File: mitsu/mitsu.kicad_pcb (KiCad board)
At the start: 2 copper layers, 8 parts, among them J1 Conn_Coaxial, J2 Conn_Coaxial

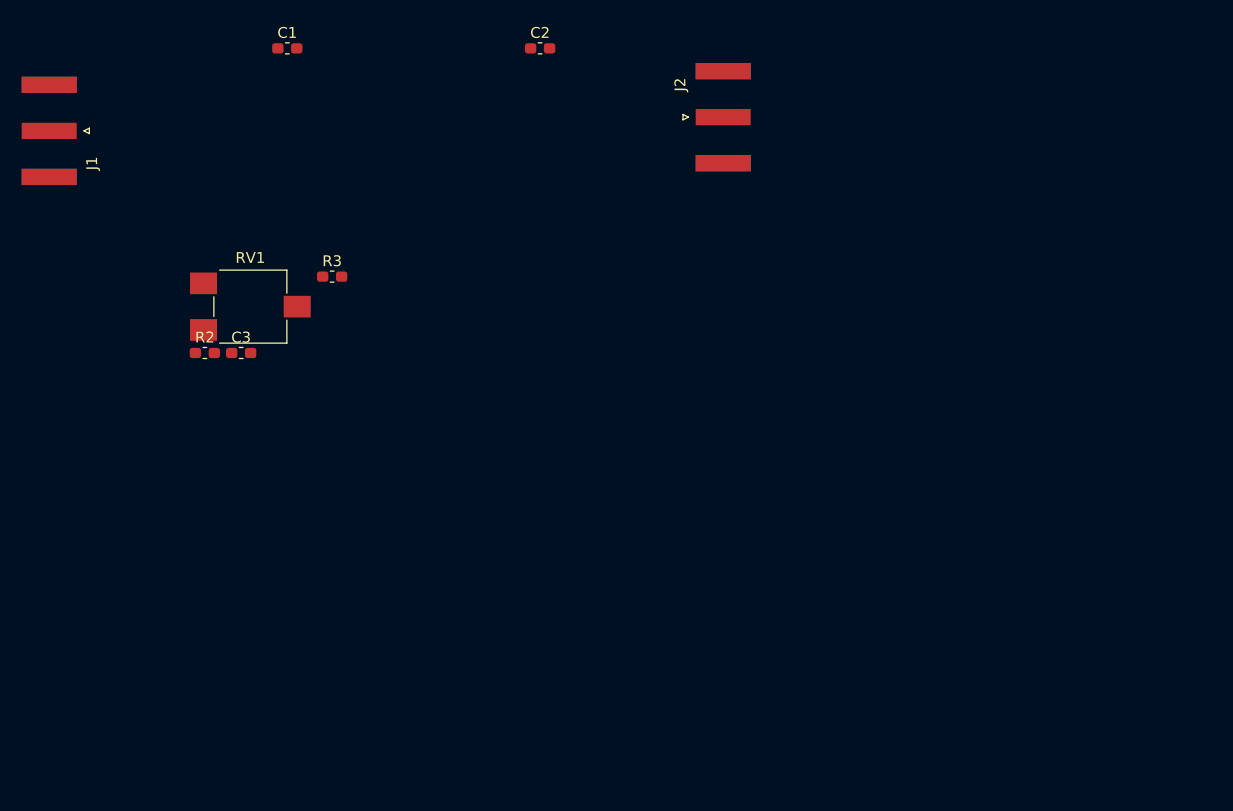
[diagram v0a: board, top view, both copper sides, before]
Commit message: fixed PA footprint
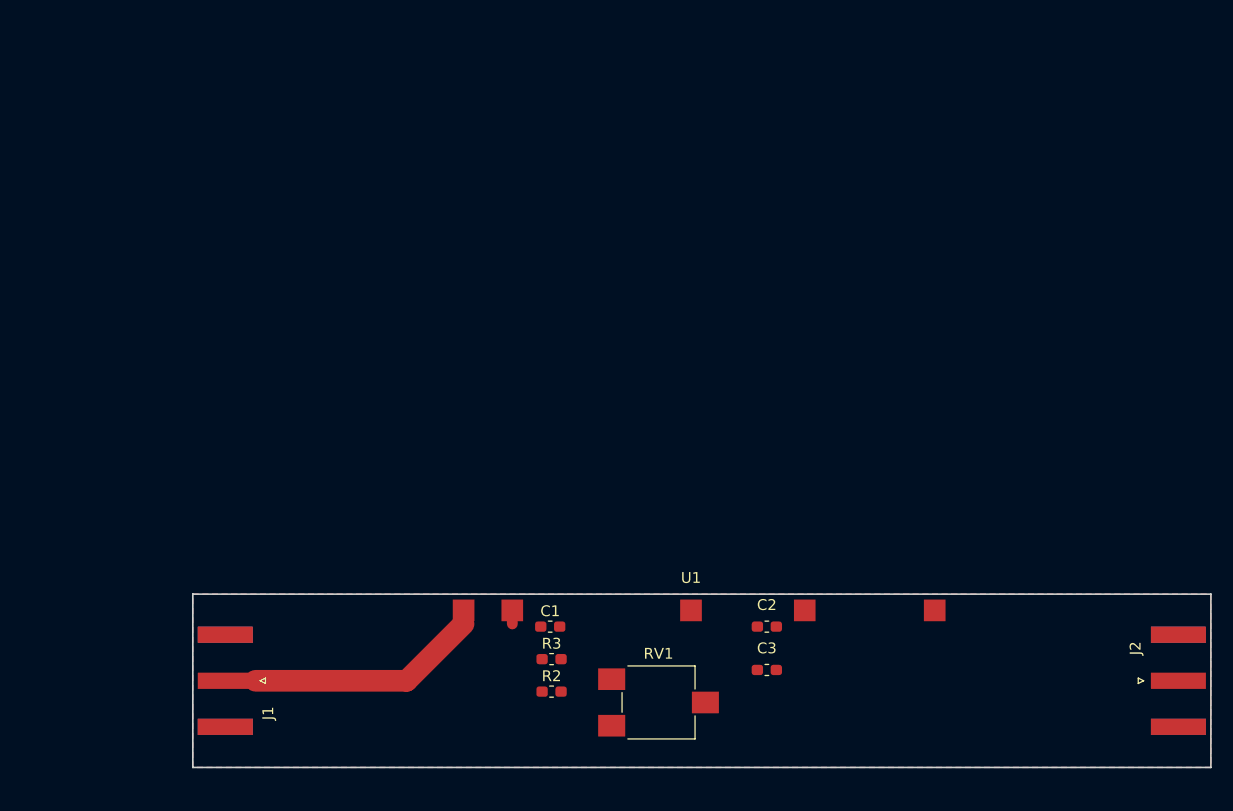
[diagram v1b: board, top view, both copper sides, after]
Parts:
- added U1: MPA, drom:MPA, F.Cu at (138.0, 105.0)
- moved J2 66.9 mm to (183.0, 113.0)
- moved C1 58.6 mm to (125.0, 108.0)
- moved C2 57.3 mm to (145.0, 108.0), turned to 180 degrees
- moved C3 56.7 mm to (145.0, 112.0), turned to 180 degrees
- moved J1 53.3 mm to (95.0, 113.0)
- moved RV1 52.5 mm to (135.0, 115.0)
- moved R2 44.7 mm to (125.1, 114.0)
- moved R3 40.7 mm to (125.1, 111.0)
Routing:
- net Net-(J1-Pad1): track 0.00 -> 25.4 mm
- net Net-(C1-Pad1): track 0.00 -> 1.25 mm
- added copper zone on B.Cu, net GNDPWR
- added copper zone on F.Cu, net GNDPWR
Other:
- board outline added: 94 x 16 mm
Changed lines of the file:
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@@
   (general
     (thickness 1.6)
-    (drawings 0)
-    (tracks 0)
+    (drawings 4)
+    (tracks 5)
     (zones 0)
-    (modules 8)
+    (modules 9)
     (nets 7)
   )
@@
     (add_net "Net-(R2-Pad2)")
   )
+  (module drom:MPA (layer F.Cu)
+    (at 138 105)
+    (descr "8-Lead Plastic PSOP, Exposed Die Pad (TI DDA0008B, see http://www.ti.com/lit/ds/symlink/lm3404.pdf)")
+    (tags "SSOP 0.50 exposed pad")
+    (attr smd)
+    (fp_text reference U1 (at 0 -1.5) (layer F.SilkS)
+      (effects (font (size 1 1) (thickness 0.15)))
+    )
+    (fp_text value MPA (at 0 -8) (layer F.Fab)
+      (effects (font (size 1 1) (thickness 0.15)))
+    )
+    (fp_text user %R (at 0 -3.5) (layer F.Fab)
+      (effects (font (size 1 1) (thickness 0.15)))
+    )
+    (fp_line (start -25 0) (end -25 -19) (layer F.Fab) (width 0.15))
+    (fp_line (start -25 -19) (end 25 -19) (layer F.Fab) (width 0.15))
+    (fp_line (start 25 -19) (end 25 0) (layer F.Fab) (width 0.15))
+    (fp_line (start 25 0) (end -25 0) (layer F.Fab) (width 0.15))
+    (fp_line (start -25 -0.5) (end -33.5 -0.5) (layer F.Fab) (width 0.15))
+    (fp_line (start -33.5 -0.5) (end -33.5 -8) (layer F.Fab) (width 0.15))
+    (fp_line (start -30.5 -18.5) (end -25 -18.5) (layer F.Fab) (width 0.15))
+    (fp_line (start -33.5 -8) (end -30 -8) (layer F.Fab) (width 0.15))
+    (fp_line (start -30 -12) (end -33.5 -12) (layer F.Fab) (width 0.15))
+    (fp_arc (start -30 -10) (end -30 -8) (angle -180) (layer F.Fab) (width 0.15))
+    (fp_line (start -33.5 -12) (end -33.5 -15.5) (layer F.Fab) (width 0.15))
+    (fp_line (start -33.5 -15.5) (end -30.5 -18.5) (layer F.Fab) (width 0.15))
+    (fp_line (start 33.5 -12) (end 30 -12) (layer F.Fab) (width 0.15))
+    (fp_arc (start 30 -10) (end 30 -12) (angle -180) (layer F.Fab) (width 0.15))
+    (fp_line (start 25 -18.5) (end 30.5 -18.5) (layer F.Fab) (width 0.15))
+    (fp_line (start 30 -8) (end 33.5 -8) (layer F.Fab) (width 0.15))
+    (fp_line (start 33.5 -0.5) (end 25 -0.5) (layer F.Fab) (width 0.15))
+    (fp_line (start 33.5 -15.5) (end 30.5 -18.5) (layer F.Fab) (width 0.15))
+    (fp_line (start 33.5 -12) (end 33.5 -15.5) (layer F.Fab) (width 0.15))
+    (fp_line (start 33.5 -0.5) (end 33.5 -8) (layer F.Fab) (width 0.15))
+    (pad 1 smd rect (at -21 1.5) (size 2 2) (layers F.Cu F.Paste F.Mask)
+      (net 2 "Net-(J1-Pad1)"))
+    (pad 2 smd rect (at -16.5 1.5) (size 2 2) (layers F.Cu F.Paste F.Mask)
+      (net 4 "Net-(C1-Pad1)"))
+    (pad 3 smd rect (at 10.5 1.5) (size 2 2) (layers F.Cu F.Paste F.Mask)
+      (net 6 +12V))
+    (pad 4 smd rect (at 22.5 1.5) (size 2 2) (layers F.Cu F.Paste F.Mask)
+      (net 3 "Net-(J2-Pad1)"))
+    (pad 5 smd rect (at 0 1.5) (size 2 2) (layers F.Cu F.Paste F.Mask)
+      (net 1 GNDPWR))
+    (model ${KISYS3DMOD}/Package_SO.3dshapes/TI_SO-PowerPAD-8.wrl
+      (at (xyz 0 0 0))
+      (scale (xyz 1 1 1))
+      (rotate (xyz 0 0 0))
+    )
+  )
   (module Capacitor_SMD:C_0603_1608Metric_Pad1.05x0.95mm_HandSolder (layer F.Cu)
-    (at 96.465001 82.735001)
+    (at 145 112 180)
     (descr "Capacitor SMD 0603 (1608 Metric), square (rectangular) end terminal, IPC_7351 nominal with elongated pad for handsoldering. (Body size source: http://www.tortai-tech.com/upload/download/2011102023233369053.pdf), generated with kicad-footprint-generator")
     (tags "capacitor handsolder")
     (attr smd)
-    (fp_text reference C3 (at 0 -1.43) (layer F.SilkS)
-      (effects (font (size 1 1) (thickness 0.15)))
-    )
-    (fp_text value C (at 0 1.43) (layer F.Fab)
+    (fp_text reference C3 (at 0 2 180) (layer F.SilkS)
+      (effects (font (size 1 1) (thickness 0.15)))
+    )
+    (fp_text value C (at -2 0 180) (layer F.Fab)
       (effects (font (size 1 1) (thickness 0.15)))
     )
@@
     (fp_line (start 1.65 -0.73) (end 1.65 0.73) (layer F.CrtYd) (width 0.05))
     (fp_line (start 1.65 0.73) (end -1.65 0.73) (layer F.CrtYd) (width 0.05))
-    (fp_text user %R (at 0 0) (layer F.Fab)
+    (fp_text user %R (at 0.534999 0 180) (layer F.Fab)
       (effects (font (size 0.4 0.4) (thickness 0.06)))
     )
-    (pad 1 smd roundrect (at -0.875 0) (size 1.05 0.95) (layers F.Cu F.Paste F.Mask) (roundrect_rratio 0.25)
+    (pad 1 smd roundrect (at -0.875 0 180) (size 1.05 0.95) (layers F.Cu F.Paste F.Mask) (roundrect_rratio 0.25)
       (net 6 +12V))
-    (pad 2 smd roundrect (at 0.875 0) (size 1.05 0.95) (layers F.Cu F.Paste F.Mask) (roundrect_rratio 0.25)
+    (pad 2 smd roundrect (at 0.875 0 180) (size 1.05 0.95) (layers F.Cu F.Paste F.Mask) (roundrect_rratio 0.25)
       (net 1 GNDPWR))
     (model ${KISYS3DMOD}/Capacitor_SMD.3dshapes/C_0603_1608Metric.wrl
@@
   )
   (module Potentiometer_SMD:Potentiometer_ACP_CA6-VSMD_Vertical (layer F.Cu)
-    (at 97.315001 78.455001)
+    (at 135 115)
     (descr "Potentiometer, vertical, ACP CA6-VSMD, http://www.acptechnologies.com/wp-content/uploads/2017/06/01-ACP-CA6.pdf")
     (tags "Potentiometer vertical ACP CA6-VSMD")
@@
   )
   (module Resistor_SMD:R_0603_1608Metric_Pad1.05x0.95mm_HandSolder (layer F.Cu)
-    (at 104.865001 75.685001)
+    (at 125.125 111)
     (descr "Resistor SMD 0603 (1608 Metric), square (rectangular) end terminal, IPC_7351 nominal with elongated pad for handsoldering. (Body size source: http://www.tortai-tech.com/upload/download/2011102023233369053.pdf), generated with kicad-footprint-generator")
     (tags "resistor handsolder")
@@
   )
   (module Resistor_SMD:R_0603_1608Metric_Pad1.05x0.95mm_HandSolder (layer F.Cu)
-    (at 93.115001 82.735001)
+    (at 125.125 114)
     (descr "Resistor SMD 0603 (1608 Metric), square (rectangular) end terminal, IPC_7351 nominal with elongated pad for handsoldering. (Body size source: http://www.tortai-tech.com/upload/download/2011102023233369053.pdf), generated with kicad-footprint-generator")
     (tags "resistor handsolder")
@@
   )
   (module Capacitor_SMD:C_0603_1608Metric_Pad1.05x0.95mm_HandSolder (layer F.Cu)
-    (at 124.065 54.61)
+    (at 145 108 180)
     (descr "Capacitor SMD 0603 (1608 Metric), square (rectangular) end terminal, IPC_7351 nominal with elongated pad for handsoldering. (Body size source: http://www.tortai-tech.com/upload/download/2011102023233369053.pdf), generated with kicad-footprint-generator")
     (tags "capacitor handsolder")
     (attr smd)
-    (fp_text reference C2 (at 0 -1.43) (layer F.SilkS)
+    (fp_text reference C2 (at 0 2 180) (layer F.SilkS)
       (effects (font (size 1 1) (thickness 0.15)))
     )
@@
       (effects (font (size 1 1) (thickness 0.15)))
     )
-    (fp_text user %R (at 0 0) (layer F.Fab)
+    (fp_text user %R (at -19.065 21.39 180) (layer F.Fab)
       (effects (font (size 0.4 0.4) (thickness 0.06)))
     )
@@
     (fp_line (start -0.8 -0.4) (end 0.8 -0.4) (layer F.Fab) (width 0.1))
     (fp_line (start -0.8 0.4) (end -0.8 -0.4) (layer F.Fab) (width 0.1))
-    (pad 2 smd roundrect (at 0.875 0) (size 1.05 0.95) (layers F.Cu F.Paste F.Mask) (roundrect_rratio 0.25)
-      (net 1 GNDPWR))
-    (pad 1 smd roundrect (at -0.875 0) (size 1.05 0.95) (layers F.Cu F.Paste F.Mask) (roundrect_rratio 0.25)
+    (pad 2 smd roundrect (at 0.875 0 180) (size 1.05 0.95) (layers F.Cu F.Paste F.Mask) (roundrect_rratio 0.25)
+      (net 1 GNDPWR))
+    (pad 1 smd roundrect (at -0.875 0 180) (size 1.05 0.95) (layers F.Cu F.Paste F.Mask) (roundrect_rratio 0.25)
       (net 6 +12V))
     (model ${KISYS3DMOD}/Capacitor_SMD.3dshapes/C_0603_1608Metric.wrl
@@
   )
   (module Capacitor_SMD:C_0603_1608Metric_Pad1.05x0.95mm_HandSolder (layer F.Cu)
-    (at 100.725 54.61)
+    (at 125 108)
     (descr "Capacitor SMD 0603 (1608 Metric), square (rectangular) end terminal, IPC_7351 nominal with elongated pad for handsoldering. (Body size source: http://www.tortai-tech.com/upload/download/2011102023233369053.pdf), generated with kicad-footprint-generator")
     (tags "capacitor handsolder")
@@
   )
   (module Connector_Coaxial:SMA_Amphenol_132289_EdgeMount (layer F.Cu)
-    (at 140.97 60.96)
+    (at 183 113)
     (descr http://www.amphenolrf.com/132289.html)
     (tags SMA)
@@
   )
   (module Connector_Coaxial:SMA_Amphenol_132289_EdgeMount (layer F.Cu)
-    (at 78.74 62.23 180)
+    (at 95 113 180)
     (descr http://www.amphenolrf.com/132289.html)
     (tags SMA)
@@
     )
   )
+  (gr_line (start 92 121) (end 92 105) (layer Edge.Cuts) (width 0.15))
+  (gr_line (start 186 121) (end 92 121) (layer Edge.Cuts) (width 0.15))
+  (gr_line (start 186 105) (end 186 121) (layer Edge.Cuts) (width 0.15))
+  (gr_line (start 92 105) (end 186 105) (layer Edge.Cuts) (width 0.15))
+  (segment (start 117 107.75) (end 111.75 113) (width 2) (layer F.Cu) (net 2))
+  (segment (start 97.79 113) (end 95 113) (width 0.25) (layer F.Cu) (net 2))
+  (segment (start 111.75 113) (end 97.79 113) (width 2) (layer F.Cu) (net 2))
+  (segment (start 117 106.5) (end 117 107.75) (width 1) (layer F.Cu) (net 2))
+  (segment (start 121.5 106.5) (end 121.5 107.75) (width 1) (layer F.Cu) (net 4))
+  (zone (net 1) (net_name GNDPWR) (layer B.Cu) (hatch edge 0.508)
+    (connect_pads (clearance 0.508))
+    (min_thickness 0.254)
+    (fill yes (arc_segments 16) (thermal_gap 0.508) (thermal_bridge_width 0.508))
+    (polygon
+      (pts
+        (xy 92 105) (xy 186 105) (xy 186 121) (xy 92 121)
+      )
+    )
+  )
+  (zone (net 1) (net_name GNDPWR) (layer F.Cu) (hatch edge 0.508)
+    (connect_pads (clearance 0.508))
+    (min_thickness 0.254)
+    (fill yes (arc_segments 16) (thermal_gap 0.508) (thermal_bridge_width 0.508))
+    (polygon
+      (pts
+        (xy 92 105) (xy 186 105) (xy 186 121) (xy 92 121)
+      )
+    )
+  )

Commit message: v1.0
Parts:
- added C10: 7.5, Capacitor_SMD:C_0805_2012Metric_Pad1.15x1.40mm_HandSolder, F.Cu at (171.0, 115.0)
- added C11: 4.7, Capacitor_SMD:C_0805_2012Metric_Pad1.15x1.40mm_HandSolder, F.Cu at (176.0, 115.0)
- added C4: 4700, Capacitor_SMD:C_0603_1608Metric_Pad1.05x0.95mm_HandSolder, F.Cu at (145.0, 106.0)
- added C5: 22.0, Capacitor_SMD:C_1210_3225Metric, F.Cu at (124.6, 109.0)
- added C6: 22.0, Capacitor_SMD:C_1210_3225Metric, F.Cu at (145.0, 109.0)
- added C7: 0.1, Capacitor_SMD:C_0603_1608Metric_Pad1.05x0.95mm_HandSolder, F.Cu at (139.0, 116.0)
- added C8: 0.1, Capacitor_SMD:C_0603_1608Metric_Pad1.05x0.95mm_HandSolder, F.Cu at (145.0, 112.0)
- added C9: 4.7, Capacitor_SMD:C_0805_2012Metric_Pad1.15x1.40mm_HandSolder, F.Cu at (165.0, 115.0)
- added L1: 11u, Inductor_SMD:L_1206_3216Metric, F.Cu at (168.0, 113.0)
- added L2: 11u, Inductor_SMD:L_1206_3216Metric, F.Cu at (174.0, 113.0)
- added R1: 300, Resistor_SMD:R_0603_1608Metric_Pad1.05x0.95mm_HandSolder, F.Cu at (100.0, 114.5)
- added R4: 15k, Resistor_SMD:R_0603_1608Metric_Pad1.05x0.95mm_HandSolder, F.Cu at (112.0, 114.5)
- added R5: 470, Resistor_SMD:R_0603_1608Metric_Pad1.05x0.95mm_HandSolder, F.Cu at (115.0, 116.1)
- added R7: 470, Resistor_SMD:R_0603_1608Metric_Pad1.05x0.95mm_HandSolder, F.Cu at (124.0, 112.0)
- added REF**: MountingHole_3.2mm_M3_ISO14580_Pad, MountingHole:MountingHole_3.2mm_M3_ISO14580_Pad, F.Cu at (108.0, 108.0)
- added REF**: MountingHole_3.2mm_M3_ISO14580_Pad, MountingHole:MountingHole_3.2mm_M3_ISO14580_Pad, F.Cu at (135.0, 108.0)
- added REF**: MountingHole_3.2mm_M3_ISO14580_Pad, MountingHole:MountingHole_3.2mm_M3_ISO14580_Pad, F.Cu at (155.0, 108.0)
- added REF**: MountingHole_3.2mm_M3_ISO14580_Pad, MountingHole:MountingHole_3.2mm_M3_ISO14580_Pad, F.Cu at (168.0, 108.0)
- added RV2: 500, Potentiometer_SMD:Potentiometer_Bourns_3214G_Horizontal, F.Cu at (133.0, 117.0)
- added U2: L78L06_SOT89, Package_TO_SOT_SMD:SOT-89-3, F.Cu at (144.0, 116.9)
- C1: value C -> 1000
- C2, C3: value C -> 4700
- R2: value 2k2 -> 18
- R3: value 2k7 -> 300
- RV1: value R_POT -> 500; footprint Potentiometer_SMD:Potentiometer_ACP_CA6-VSMD_Vertical -> Potentiometer_SMD:Potentiometer_Bourns_3214G_Horizontal
- moved C2 28.2 mm to (118.0, 116.1), turned to 90 degrees
- moved R2 22.1 mm to (103.0, 113.0), turned to 180 degrees
- moved C3 21.8 mm to (124.0, 106.0), turned to 0 degrees
- moved R3 19.4 mm to (106.0, 114.5), turned to 270 degrees
- moved C1 16.8 mm to (109.0, 113.0), turned to 180 degrees
- moved RV1 11.2 mm to (124.0, 117.0), turned to 180 degrees
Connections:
- C1 pad 2: GNDPWR -> Net-(C1-Pad2)
- C2 pad 1: +12V -> Net-(C2-Pad1)
- C3 pad 1: +12V -> Net-(C3-Pad1)
- J2 pad 1: Net-(J2-Pad1) -> Net-(C11-Pad2)
- R2 pad 1: Net-(C1-Pad1) -> Net-(C1-Pad2)
- R2 pad 2: Net-(R2-Pad2) -> Net-(J1-Pad1)
- R3 pad 1: Net-(C1-Pad1) -> Net-(C1-Pad2)
- RV1 pad 1: Net-(R2-Pad2) -> Net-(C7-Pad1)
- RV1 pad 2: +12V -> Net-(C7-Pad1)
- RV1 pad 3: +12V -> Net-(C2-Pad1)
- U1 pad 1: Net-(J1-Pad1) -> Net-(C1-Pad1)
- U1 pad 2: Net-(C1-Pad1) -> Net-(C3-Pad1)
- U1 pad 4: Net-(J2-Pad1) -> Net-(C9-Pad2)
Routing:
- net +12V: track 0.00 -> 37.7 mm
- net Net-(C7-Pad1): track 0.00 -> 23.6 mm
- net Net-(C3-Pad1): track 0.00 -> 21.9 mm
- net Net-(J1-Pad1): track 25.4 -> 7.12 mm
- net Net-(C11-Pad2): track 0.00 -> 11.6 mm
- net Net-(C1-Pad1): track 1.25 -> 12.2 mm
- net Net-(C2-Pad1): track 0.00 -> 10.5 mm
- net Net-(C9-Pad2): track 0.00 -> 10.4 mm
- net Net-(C1-Pad2): track 0.00 -> 4.25 mm
- net Net-(C10-Pad2): track 0.00 -> 2.00 mm
- net GNDPWR: vias 0 -> 174
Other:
- net class 50om added: clearance 0.8, trace_width 2, via_dia 1, via_drill 0.8
- net class Default: trace_width 0.25 -> 0.5
- board text added: "900M PA45"
- board text added: "AI6YP"

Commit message: final changes for mitsu v1
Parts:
- removed REF** (x4): MountingHole_3.2mm_M3_ISO14580_Pad, MountingHole:MountingHole_3.2mm_M3_ISO14580_Pad
- added J3: Conn_01x04_Male, Connector_PinHeader_2.54mm:PinHeader_1x02_P2.54mm_Vertical_SMD_Pin1Right, F.Cu at (142.5, 117.0)
- added MH1: MountingHole, MountingHole:MountingHole_3.2mm_M3_ISO14580_Pad, F.Cu at (108.0, 108.0)
- added MH2: MountingHole, MountingHole:MountingHole_3.2mm_M3_ISO14580_Pad, F.Cu at (135.0, 108.0)
- added MH3: MountingHole, MountingHole:MountingHole_3.2mm_M3_ISO14580_Pad, F.Cu at (155.0, 108.0)
- added MH4: MountingHole, MountingHole:MountingHole_3.2mm_M3_ISO14580_Pad, F.Cu at (168.0, 108.0)
- C1, C2, C3, C4, C7, C8: footprint Capacitor_SMD:C_0603_1608Metric_Pad1.05x0.95mm_HandSolder -> Capacitor_SMD:C_0805_2012Metric_Pad1.15x1.40mm_HandSolder
- R1, R2, R3, R4, R5, R7: footprint Resistor_SMD:R_0603_1608Metric_Pad1.05x0.95mm_HandSolder -> Resistor_SMD:R_0805_2012Metric_Pad1.15x1.40mm_HandSolder
- moved C7 9.66 mm to (130.0, 112.5), turned to 90 degrees
- moved U2 9.05 mm to (135.0, 117.8), turned to 90 degrees
- moved RV2 6.08 mm to (127.0, 118.0)
- moved R5 5.34 mm to (110.0, 118.0), turned to 90 degrees
- moved RV1 5.10 mm to (119.0, 118.0)
- moved C2 4.42 mm to (114.0, 118.0), turned to 270 degrees
- moved C11 1.13 mm to (177.0, 114.5)
- moved C9 0.55 mm to (165.0, 114.5)
- moved C10 0.50 mm to (171.0, 114.5)
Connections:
- U2 pad 1: +12V -> Net-(C7-Pad1)
- U2 pad 3: Net-(C7-Pad1) -> +12V
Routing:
- net +12V: track 37.7 -> 54.8 mm
- net GNDPWR: track 0.00 -> 3.42 mm, vias 174 -> 161
- net Net-(C2-Pad1): track 10.5 -> 7.80 mm
- net Net-(C3-Pad1): track 21.9 -> 20.9 mm
- net Net-(C1-Pad1): track 12.2 -> 11.4 mm
- net Net-(C7-Pad1): track 23.6 -> 23.1 mm
